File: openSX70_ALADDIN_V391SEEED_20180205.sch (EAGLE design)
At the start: 46 parts, among them J1 GND, Q1 2N7002, Q2 2N7002, U1 ATMEGA328P_TQFP, U3 BH1750FVI-TR, Y1 CSTCE8M00G52Z-R0

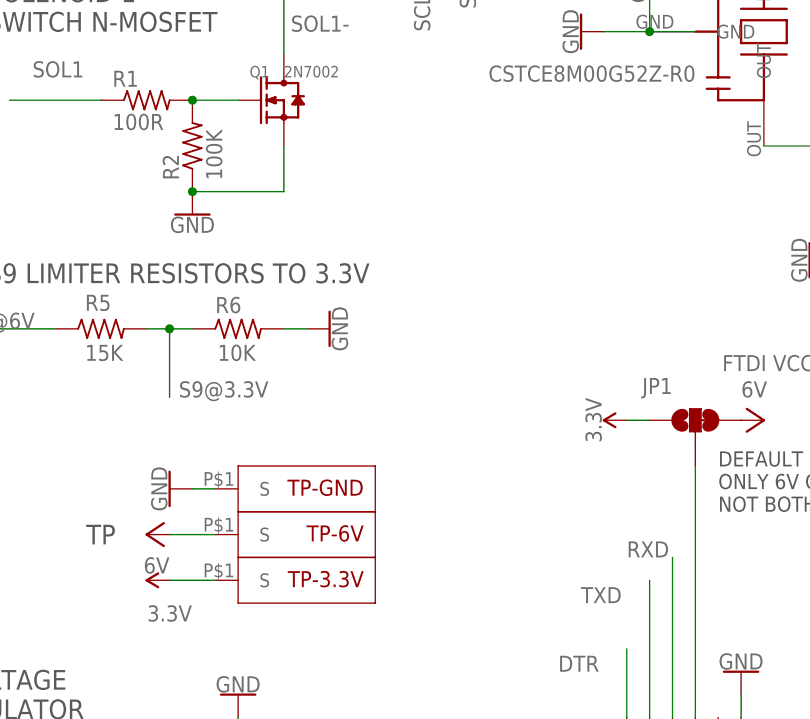
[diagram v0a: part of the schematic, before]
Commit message: Working on an ICSP header
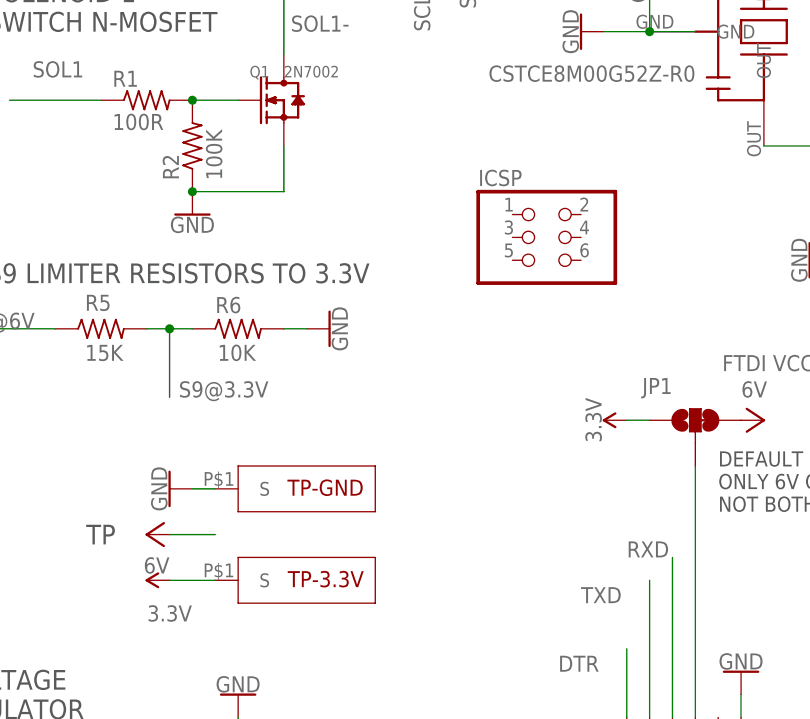
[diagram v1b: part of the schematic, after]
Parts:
- removed TP-6V: SX70-S-PAD-NEW, openSX70:SX70-S-PAD-NEW
- added ICSP: (no value), pinhead:PINHD-2X3
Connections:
- net 6V: no longer TP-6V.S
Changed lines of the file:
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@@
 <part name="D1" library="zetex" library_urn="urn:adsk.eagle:library:418" deviceset="D" device="SOD323" package3d_urn="urn:adsk.eagle:package:30992/1" value="1N4148WSF"/>
 <part name="P+8" library="openSX70" deviceset="VCC" device="" value="6V"/>
-<part name="TP-6V" library="openSX70" deviceset="SX70-S-PAD-NEW" device=""/>
 <part name="TP-3.3V" library="openSX70" deviceset="SX70-S-PAD-NEW" device=""/>
 <part name="TP-GND" library="openSX70" deviceset="SX70-S-PAD-NEW" device=""/>
@@
 <part name="SCL" library="testpad" library_urn="urn:adsk.eagle:library:385" deviceset="PTR1" device="TP08R" package3d_urn="urn:adsk.eagle:package:27956/1" value="PTR1TP08R"/>
 <part name="J1" library="con-omron" library_urn="urn:adsk.eagle:library:167" deviceset="XF2*-06?" device="25-1" package3d_urn="urn:adsk.eagle:package:9011/1" technology="L" value="GND"/>
+<part name="ICSP" library="pinhead" library_urn="urn:adsk.eagle:library:325" deviceset="PINHD-2X3" device="" package3d_urn="urn:adsk.eagle:package:22462/2"/>
 </parts>
 <sheets>
@@
 </instance>
 <instance part="P+8" gate="VCC" x="182.88" y="50.8" rot="R90"/>
-<instance part="TP-6V" gate="G$1" x="83.82" y="40.64" rot="R180"/>
 <instance part="TP-3.3V" gate="G$1" x="83.82" y="35.56" rot="R180"/>
 <instance part="TP-GND" gate="G$1" x="83.82" y="45.72" rot="R180"/>
@@
 <attribute name="NAME" x="121.158" y="15.24" size="1.524" layer="95" rot="R270"/>
 </instance>
+<instance part="ICSP" gate="A" x="111.76" y="73.66"/>
 </instances>
 <busses>
@@
 <segment>
 <pinref part="P+9" gate="VCC" pin="6V"/>
-<pinref part="TP-6V" gate="G$1" pin="S"/>
 <wire x1="71.12" y1="40.64" x2="76.2" y2="40.64" width="0.1524" layer="91"/>
 </segment>
